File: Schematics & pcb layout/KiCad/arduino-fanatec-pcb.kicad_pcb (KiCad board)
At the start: 2 copper layers, 67.3 x 80 mm, 19 parts, among them J1 SPI Connector 01x08_Female, J2 TM1637 4 digit Display connec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, J3 Breakout Connector 02x18_Odd_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, U1 Simple_Chinese_Logic_level_sh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

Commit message: wip
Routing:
- net GND: track 286.8 -> 276.6 mm
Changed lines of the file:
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@@
     (thickness 1.6)
     (drawings 10)
-    (tracks 315)
+    (tracks 314)
     (zones 0)
     (modules 19)
@@
   (segment (start 101.6 95.25) (end 102.937919 95.25) (width 0.7) (layer B.Cu) (net 13))
   (segment (start 102.937919 95.25) (end 115.637919 82.55) (width 0.7) (layer B.Cu) (net 13))
-  (segment (start 58.487919 90.17) (end 56.896 88.578081) (width 0.7) (layer B.Cu) (net 40))
-  (segment (start 59.69 90.17) (end 58.487919 90.17) (width 0.7) (layer B.Cu) (net 40))
-  (segment (start 56.896 80.264) (end 57.15 80.01) (width 0.7) (layer B.Cu) (net 40))
-  (segment (start 57.15 80.01) (end 60.325 80.01) (width 0.7) (layer B.Cu) (net 40))
-  (segment (start 56.896 88.578081) (end 56.896 80.264) (width 0.7) (layer B.Cu) (net 40))
-  (segment (start 60.325 80.01) (end 62.23 81.915) (width 0.7) (layer B.Cu) (net 40))
-  (segment (start 64.135 81.915) (end 67.31 81.915) (width 0.7) (layer B.Cu) (net 40))
-  (segment (start 62.23 81.915) (end 64.135 81.915) (width 0.7) (layer B.Cu) (net 40))
-  (segment (start 64.135 81.915) (end 64.164438 81.944438) (width 0.7) (layer B.Cu) (net 40))
-  (segment (start 64.164438 81.944438) (end 64.164438 84.425562) (width 0.7) (layer B.Cu) (net 40))
-  (segment (start 64.135 84.396124) (end 64.164438 84.425562) (width 0.25) (layer B.Cu) (net 40))
   (via (at 98.425 100.33) (size 1.6) (drill 0.8) (layers F.Cu B.Cu) (net 16))
   (segment (start 101.6 100.33) (end 98.425 100.33) (width 0.7) (layer B.Cu) (net 16))
-  (via (at 64.164438 84.425562) (size 1.6) (drill 0.8) (layers F.Cu B.Cu) (net 40))
   (segment (start 119.38 67.31) (end 119.38 110.49) (width 0.7) (layer B.Cu) (net 18))
   (segment (start 119.38 53.34) (end 119.38 67.31) (width 0.7) (layer B.Cu) (net 18))
@@
   (segment (start 62.659999 87.149999) (end 61.749999 88.059999) (width 0.7) (layer F.Cu) (net 18))
   (segment (start 67.31 93.98) (end 65.25 93.98) (width 0.7) (layer B.Cu) (net 18))
-  (segment (start 67.31 93.98) (end 77.47 93.98) (width 0.7) (layer F.Cu) (net 18))
   (segment (start 59.119999 38.799999) (end 58.42 38.1) (width 0.7) (layer B.Cu) (net 18))
   (segment (start 61.640001 41.320001) (end 59.119999 38.799999) (width 0.7) (layer B.Cu) (net 18))
@@
   (segment (start 105.950023 107.326965) (end 105.950023 102.397896) (width 0.7) (layer B.Cu) (net 39))
   (segment (start 86.36 87.63) (end 93.919978 95.189978) (width 0.7) (layer B.Cu) (net 39))
+  (segment (start 58.487919 90.17) (end 56.896 88.578081) (width 0.7) (layer B.Cu) (net 40))
+  (segment (start 59.69 90.17) (end 58.487919 90.17) (width 0.7) (layer B.Cu) (net 40))
+  (segment (start 56.896 80.264) (end 57.15 80.01) (width 0.7) (layer B.Cu) (net 40))
+  (segment (start 57.15 80.01) (end 60.325 80.01) (width 0.7) (layer B.Cu) (net 40))
+  (segment (start 56.896 88.578081) (end 56.896 80.264) (width 0.7) (layer B.Cu) (net 40))
+  (segment (start 60.325 80.01) (end 62.23 81.915) (width 0.7) (layer B.Cu) (net 40))
+  (segment (start 64.135 81.915) (end 67.31 81.915) (width 0.7) (layer B.Cu) (net 40))
+  (segment (start 62.23 81.915) (end 64.135 81.915) (width 0.7) (layer B.Cu) (net 40))
+  (segment (start 64.135 81.915) (end 64.164438 81.944438) (width 0.7) (layer B.Cu) (net 40))
+  (segment (start 64.164438 81.944438) (end 64.164438 84.425562) (width 0.7) (layer B.Cu) (net 40))
+  (segment (start 64.135 84.396124) (end 64.164438 84.425562) (width 0.25) (layer B.Cu) (net 40))
+  (via (at 64.164438 84.425562) (size 1.6) (drill 0.8) (layers F.Cu B.Cu) (net 40))
   (zone (net 18) (net_name GND) (layer B.Cu) (hatch edge 0.508)
     (connect_pads (clearance 0.508))

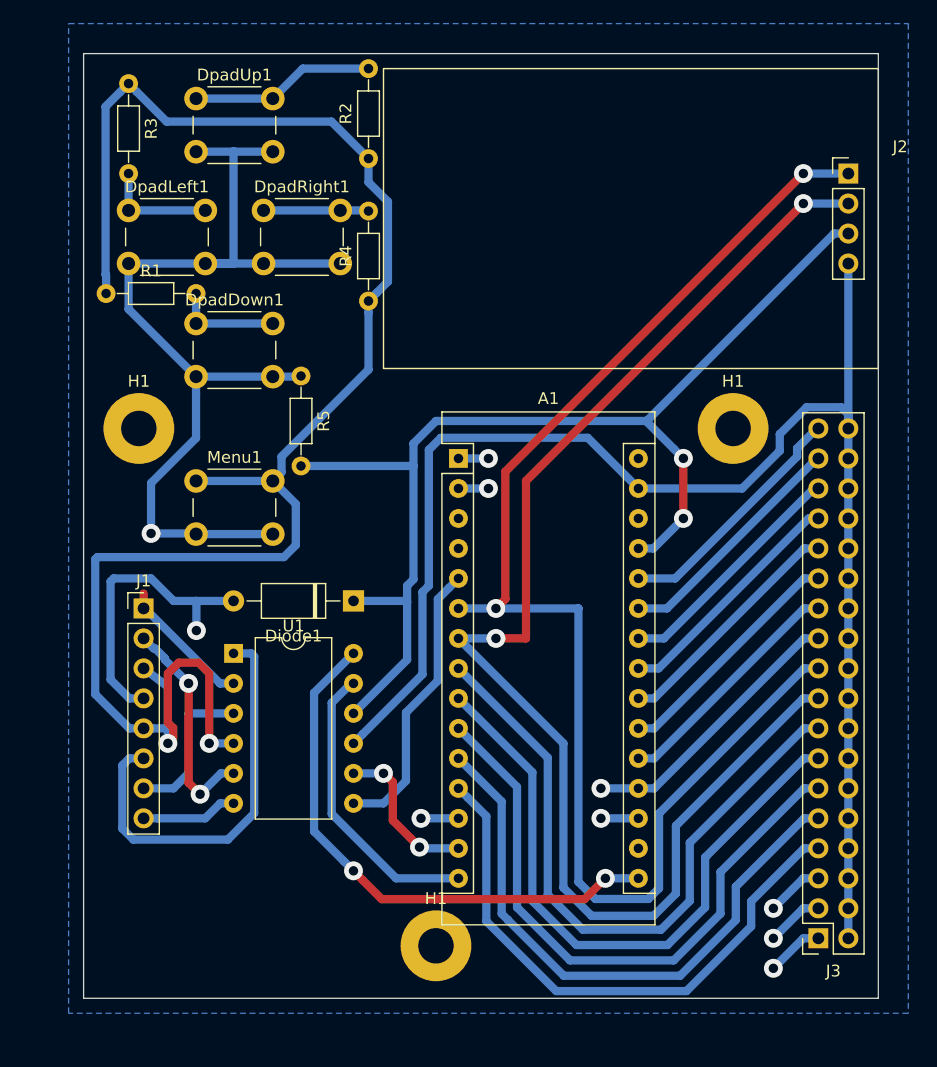
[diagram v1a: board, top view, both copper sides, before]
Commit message: updated PCB layout and schematics, including Dpad, Alphanumeric display, buttons, Diode - and many bug fixes
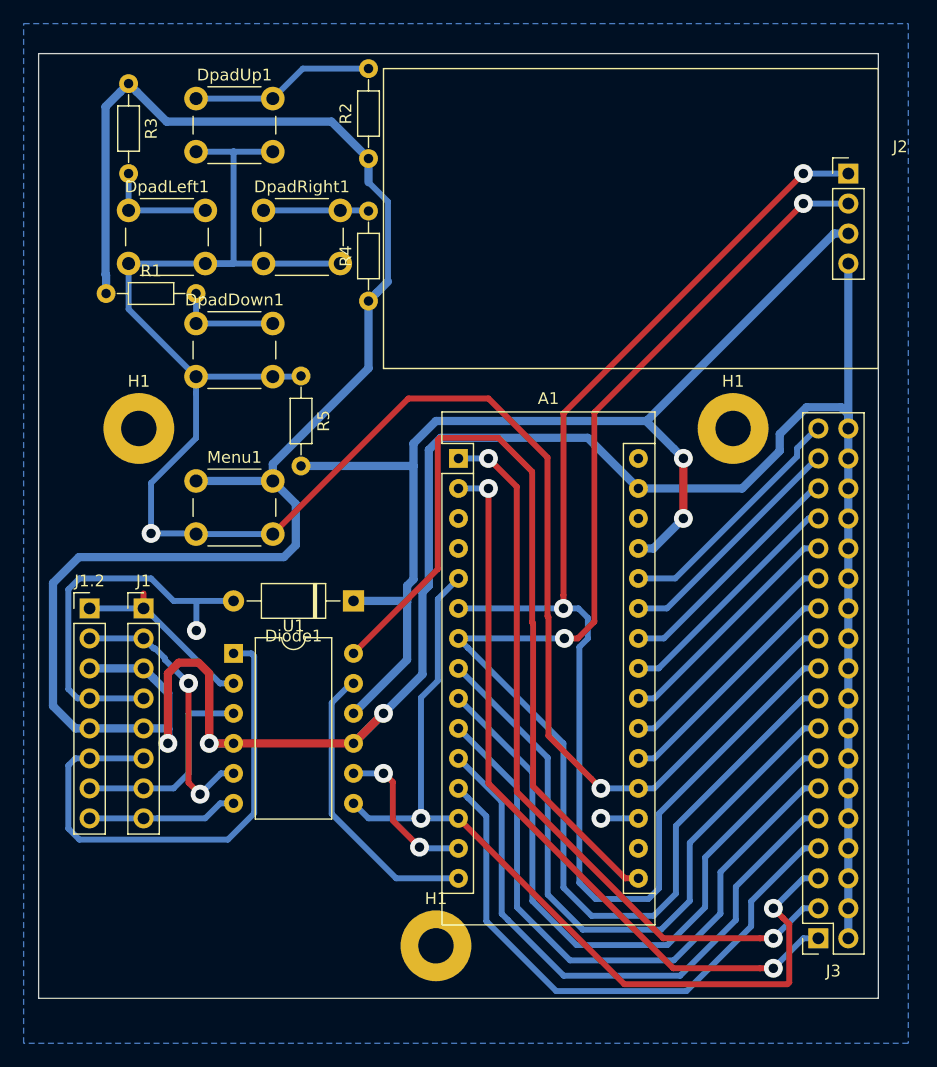
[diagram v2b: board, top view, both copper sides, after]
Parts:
- added J1.2: Extra pin breakout, Connector_PinHeader_2.54mm:PinHeader_1x08_P2.54mm_Vertical, F.Cu at (55.1, 82.5)
- J1: value SPI Connector 01x08_Female -> SPI Connector 01x08_Male
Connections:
- A1 pad 5: Net-(A1-Pad5) -> /D10
- U1 pad 7: Net-(A1-Pad5) -> /D10
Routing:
- net /D10: track 8.04 -> 76.6 mm
- net /Dpad: track 106.1 -> 166.1 mm
- net /D1: track 7.40 -> 63.5 mm
- net /D0: track 7.40 -> 63.0 mm
- net GND: track 276.6 -> 302.5 mm, vias 2 -> 3
- net Net-(A1-Pad5): track 24.2 -> 0.00 mm
- net Net-(A1-Pad16): track 47.0 -> 69.1 mm, vias 2 -> 0
- net Net-(J1-Pad6): track 35.0 -> 44.2 mm
- net Net-(Diode1-Pad2): track 25.6 -> 32.9 mm
- net Net-(J1-Pad8): track 8.15 -> 12.7 mm
- net Net-(J1-Pad7): track 13.2 -> 17.8 mm
- net Net-(J1-Pad2): track 18.8 -> 23.4 mm
- net Net-(J1-Pad1): track 11.5 -> 16.1 mm
- net /TM_D: track 114.4 -> 117.0 mm
- net /TM_CLK: track 117.5 -> 115.7 mm
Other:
- board size 67.3 x 80 mm -> 71.1 x 80 mm
